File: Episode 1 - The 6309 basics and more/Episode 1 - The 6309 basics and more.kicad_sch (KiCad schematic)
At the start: 0 parts

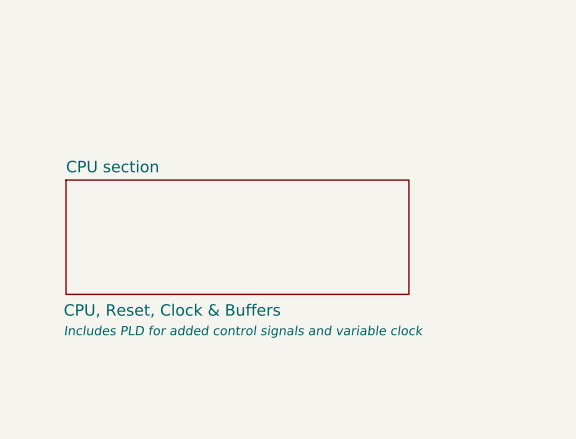
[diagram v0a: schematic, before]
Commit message: Updating PCB option
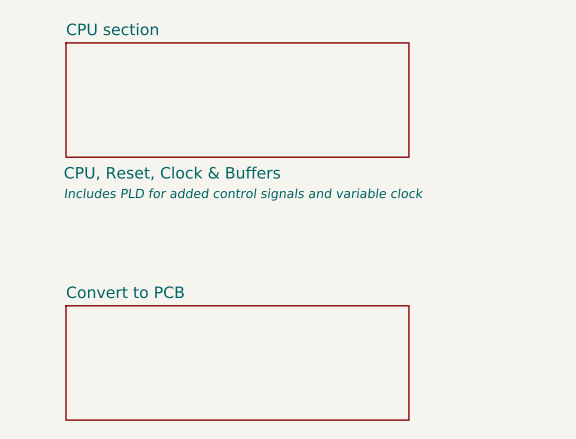
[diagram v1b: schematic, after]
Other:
- added sheet Convert to PCB (PCB.kicad_sch)
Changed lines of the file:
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@@
 	(generator "eeschema")
 	(generator_version "8.0")
-	(paper "USLegal")
+	(paper "USLetter")
 	(title_block
 		(title "LogicSpark'09 Revisited")
@@
 	)
 	(sheet
-		(at 25.4 38.1)
+		(at 25.4 22.86)
 		(size 38.1 12.7)
 		(stroke
@@
 		)
 		(property "Sheetname" "CPU section"
-			(at 25.4 37.3884 0)
+			(at 25.4 22.1484 0)
 			(effects
 				(font
@@
 		)
 		(property "Sheetfile" "CPU.kicad_sch"
-			(at 25.4 51.3846 0)
+			(at 25.4 36.1446 0)
 			(effects
 				(font
@@
 		)
 		(property "Title" "CPU, Reset, Clock & Buffers"
-			(at 25.146 52.578 0)
+			(at 25.146 37.338 0)
 			(do_not_autoplace yes)
 			(effects
@@
 		)
 		(property "More" "Includes PLD for added control signals and variable clock"
-			(at 25.146 54.864 0)
+			(at 25.146 39.624 0)
 			(effects
 				(font
@@
 				)
 			)
+		)
+	)
+	(sheet
+		(at 25.4 52.07)
+		(size 38.1 12.7)
+		(fields_autoplaced yes)
+		(stroke
+			(width 0.1524)
+			(type solid)
+		)
+		(fill
+			(color 0 0 0 0.0000)
+		)
+		(property "Sheetname" "Convert to PCB"
+			(at 25.4 51.3584 0)
+			(effects
+				(font
+					(size 1.27 1.27)
+				)
+				(justify left bottom)
+			)
+		)
+		(property "Sheetfile" "PCB.kicad_sch"
+			(at 25.4 65.3546 0)
+			(effects
+				(font
+					(size 1.27 1.27)
+				)
+				(justify left top)
+				(hide yes)
+			)
+		)
+		(instances
+			(project "Episode 1 - The 6309 basics and more"
+				(path "/5aeeb5e8-9d85-437a-bcb8-c2a3d321d580"
+					(page "3")
+				)
+			)

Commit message: PLD coding
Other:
- removed sheet Convert to PCB
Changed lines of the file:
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@@
 	)
 	(sheet
-		(at 25.4 22.86)
+		(at 20.32 22.86)
 		(size 38.1 12.7)
 		(stroke
@@
 		)
 		(property "Sheetname" "CPU section"
-			(at 25.4 22.1484 0)
+			(at 20.32 22.1484 0)
 			(effects
 				(font
@@
 		)
 		(property "Sheetfile" "CPU.kicad_sch"
-			(at 25.4 36.1446 0)
+			(at 20.32 36.1446 0)
 			(effects
 				(font
@@
 		)
 		(property "Title" "CPU, Reset, Clock & Buffers"
-			(at 25.146 37.338 0)
+			(at 20.066 37.338 0)
 			(do_not_autoplace yes)
 			(effects
@@
 		)
 		(property "More" "Includes PLD for added control signals and variable clock"
-			(at 25.146 39.624 0)
+			(at 20.066 39.624 0)
 			(effects
 				(font
@@
 				)
 			)
-		)
-	)
-	(sheet
-		(at 25.4 52.07)
-		(size 38.1 12.7)
-		(fields_autoplaced yes)
-		(stroke
-			(width 0.1524)
-			(type solid)
-		)
-		(fill
-			(color 0 0 0 0.0000)
-		)
-		(property "Sheetname" "Convert to PCB"
-			(at 25.4 51.3584 0)
-			(effects
-				(font
-					(size 1.27 1.27)
-				)
-				(justify left bottom)
-			)
-		)
-		(property "Sheetfile" "PCB.kicad_sch"
-			(at 25.4 65.3546 0)
-			(effects
-				(font
-					(size 1.27 1.27)
-				)
-				(justify left top)
-				(hide yes)
-			)
-		)
-		(instances
-			(project "Episode 1 - The 6309 basics and more"
-				(path "/5aeeb5e8-9d85-437a-bcb8-c2a3d321d580"
-					(page "3")
-				)
-			)
